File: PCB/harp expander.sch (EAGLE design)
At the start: 132 parts, among them IC1 XMEGA-A1TQFP, IC14 SN74LVC1G125DBVT, IC2 USBLC6-2SC6, IC3 FT232RL, IC4 TLV70033DDCR, IC5 TLV70033DDCR, IC6 SI8610BC-B-IS, IC7 SN74LVC1G125DBVT, T10 BC850, T11 BC850, T12 BC850, T13 BC850, T2 BC850, T3 BC850, T4 BC850, T5 BC850, T6 BC850, T7 BC850, T8 BC850, T9 BC850, U1 744245X, U2 744245X

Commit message: Minor corrections.
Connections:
- net IO_BUTTON0 renamed AUX_IN0
- net IO_BUTTON1 renamed AUX_IN1
- net PD0 renamed IO4_UC
- net PD1 renamed IO3_UC
- net PD2 renamed IO2_UC
- net PD3 renamed IO1_UC
- net PD4 renamed IO0_UC
- net PE0 renamed IO5_UC
- net PE1 renamed IO6_UC
- net PE2 renamed IO7_UC
- net PE3 renamed IO8_UC
- net PE4 renamed IO9_UC
- net USER_BUTTON_1 renamed AUX_IN1_UC
- removed net USER_BUTTON_0: IC1.PA1(ADCA1), IC14A.O
- new net AUX_IN0_UC: IC1.PA1(ADCA1), IC1.PE2(OC0C/RXD0), IC14A.O
- new net N$166: IC1.PF6(RXD1/MISO)

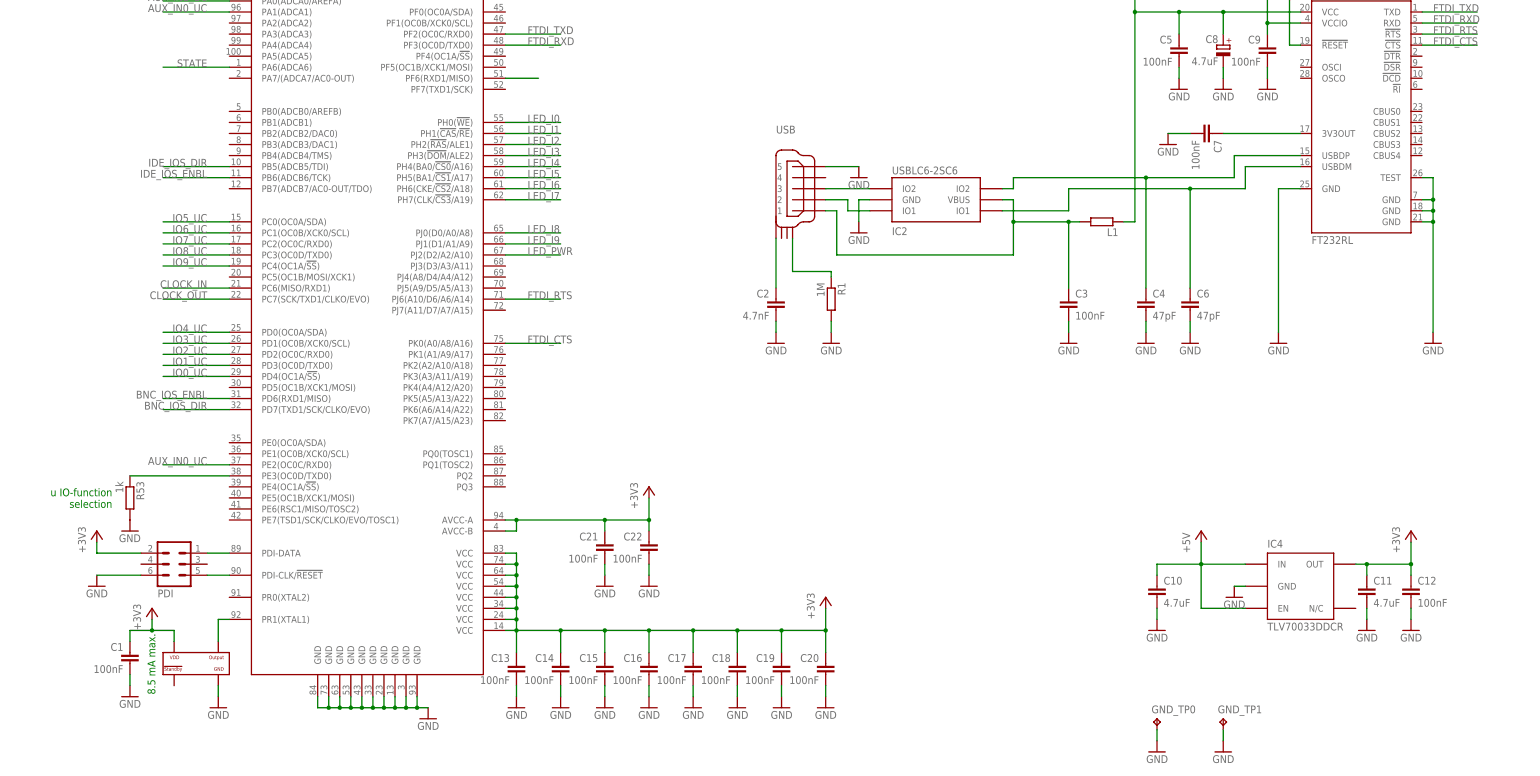
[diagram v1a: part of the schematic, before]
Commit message: Added ability to connect to a Teensy/Arduino and to read rotary encoders.
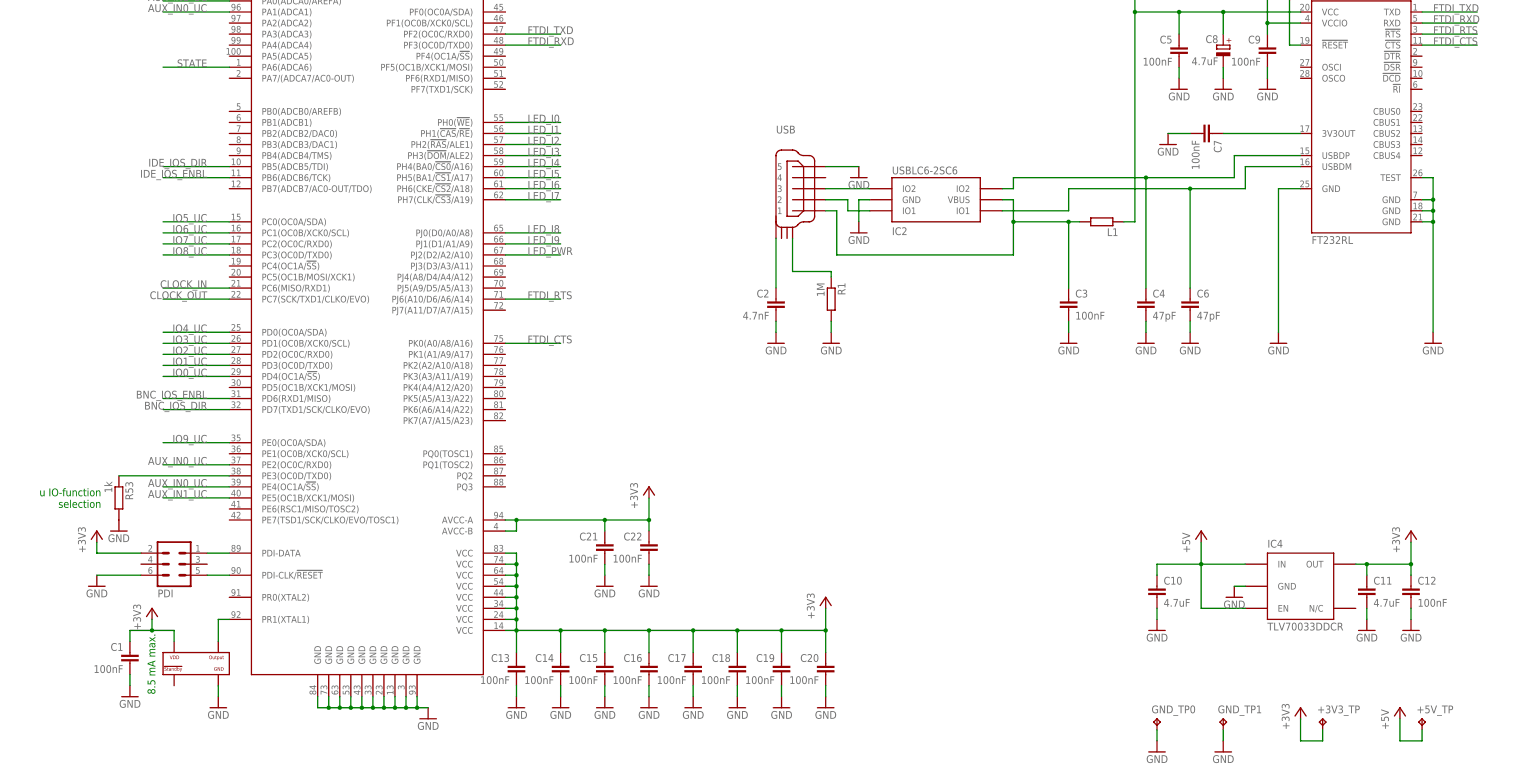
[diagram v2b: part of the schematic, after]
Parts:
- added +3V3_TP, +5V_TP: TPPAD1-13, testpad:TPPAD1-13
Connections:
- removed net N$166: IC1.PF6(RXD1/MISO)
- net +3V3: now also +3V3_TP.TP
- net +5V: now also +5V_TP.TP
- net AUX_IN0_UC: now also IC1.PE4(OC1A/!SS!)
- net AUX_IN1_UC: now also IC1.PE5(OC1B/XCK1/MOSI)
- net IO9_UC: now also IC1.PE0(OC0A/SDA); no longer IC1.PC4(OC1A/!SS!)
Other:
- moved on the sheet: R53
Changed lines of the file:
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@@
 </part>
 <part name="GND61" library="supply1" deviceset="GND" device=""/>
+<part name="+3V3_TP" library="testpad" library_urn="urn:adsk.eagle:library:385" deviceset="TP" device="PAD1-13" package3d_urn="urn:adsk.eagle:package:27946/1">
+<attribute name="MPN" value="n.a."/>
+</part>
+<part name="+3V19" library="supply1" library_urn="urn:adsk.eagle:library:371" deviceset="+3V3" device=""/>
+<part name="+5V_TP" library="testpad" library_urn="urn:adsk.eagle:library:385" deviceset="TP" device="PAD1-13" package3d_urn="urn:adsk.eagle:package:27946/1">
+<attribute name="MPN" value="n.a."/>
+</part>
+<part name="P+5" library="supply1" deviceset="+5V" device=""/>
 </parts>
 <sheets>
@@
 <text x="54.102" y="51.308" size="1.778" layer="91" rot="R90">8.5 mA max.</text>
 <text x="657.86" y="332.74" size="1.778" layer="91">SBH11-PBPC-D05-RA-BK</text>
-<text x="44.196" y="94.234" size="1.778" layer="91" align="bottom-right">u IO-function
+<text x="41.656" y="94.234" size="1.778" layer="91" align="bottom-right">u IO-function
 selection</text>
 </plain>
@@
 <attribute name="VALUE" x="548.64" y="274.32" size="1.778" layer="96"/>
 </instance>
-<instance part="R53" gate="G$1" x="48.26" y="96.52" smashed="yes" rot="R270">
-<attribute name="NAME" x="49.7586" y="100.33" size="1.778" layer="95" rot="R270"/>
-<attribute name="VALUE" x="44.958" y="100.33" size="1.778" layer="96" rot="R270"/>
-<attribute name="MPN" x="48.26" y="96.52" size="1.778" layer="96" rot="R270" display="off"/>
+<instance part="R53" gate="G$1" x="45.72" y="96.52" smashed="yes" rot="R270">
+<attribute name="NAME" x="47.2186" y="100.33" size="1.778" layer="95" rot="R270"/>
+<attribute name="VALUE" x="42.418" y="100.33" size="1.778" layer="96" rot="R270"/>
+<attribute name="MPN" x="45.72" y="96.52" size="1.778" layer="96" rot="R270" display="off"/>
+</instance>
+<instance part="GND61" gate="1" x="45.72" y="88.9" smashed="yes">
+<attribute name="VALUE" x="43.18" y="86.36" size="1.778" layer="96"/>
+</instance>
+<instance part="+3V3_TP" gate="G$1" x="322.58" y="45.72" smashed="yes">
+<attribute name="NAME" x="321.31" y="46.99" size="1.778" layer="95"/>
+<attribute name="TP_SIGNAL_NAME" x="323.85" y="44.45" size="1.778" layer="97"/>
+<attribute name="MPN" x="322.58" y="45.72" size="1.778" layer="96" display="off"/>
+</instance>
+<instance part="+3V19" gate="G$1" x="317.5" y="48.26" smashed="yes">
+<attribute name="VALUE" x="314.96" y="43.18" size="1.778" layer="96" rot="R90"/>
+</instance>
+<instance part="+5V_TP" gate="G$1" x="345.44" y="45.72" smashed="yes">
+<attribute name="NAME" x="344.17" y="46.99" size="1.778" layer="95"/>
+<attribute name="TP_SIGNAL_NAME" x="346.71" y="44.45" size="1.778" layer="97"/>
+<attribute name="MPN" x="345.44" y="45.72" size="1.778" layer="96" display="off"/>
 </instance>
-<instance part="GND61" gate="1" x="48.26" y="88.9" smashed="yes">
-<attribute name="VALUE" x="45.72" y="86.36" size="1.778" layer="96"/>
+<instance part="P+5" gate="1" x="340.36" y="48.26" smashed="yes">
+<attribute name="VALUE" x="337.82" y="43.18" size="1.778" layer="96" rot="R90"/>
 </instance>
 </instances>
@@
 <junction x="492.76" y="421.64"/>
 </segment>
+<segment>
+<pinref part="P+5" gate="1" pin="+5V"/>
+<wire x1="340.36" y1="45.72" x2="340.36" y2="40.64" width="0.1524" layer="91"/>
+<wire x1="340.36" y1="40.64" x2="345.44" y2="40.64" width="0.1524" layer="91"/>
+<pinref part="+5V_TP" gate="G$1" pin="TP"/>
+<wire x1="345.44" y1="40.64" x2="345.44" y2="43.18" width="0.1524" layer="91"/>
+</segment>
 </net>
 <net name="N$2" class="0">
@@
 <label x="66.04" y="210.82" size="1.778" layer="95" rot="MR0"/>
 </segment>
+<segment>
+<pinref part="IC1" gate="G$1" pin="PE5(OC1B/XCK1/MOSI)"/>
+<wire x1="71.12" y1="96.52" x2="55.88" y2="96.52" width="0.1524" layer="91"/>
+<label x="66.04" y="96.52" size="1.778" layer="95" rot="MR0"/>
+</segment>
 </net>
 <net name="AUX_IN0_UC" class="0">
@@
 <label x="66.04" y="104.14" size="1.778" layer="95" rot="MR0"/>
 </segment>
+<segment>
+<pinref part="IC1" gate="G$1" pin="PE4(OC1A/!SS!)"/>
+<wire x1="71.12" y1="99.06" x2="55.88" y2="99.06" width="0.1524" layer="91"/>
+<label x="66.04" y="99.06" size="1.778" layer="95" rot="MR0"/>
+</segment>
 </net>
 <net name="+3V3" class="0">
@@
 <wire x1="500.38" y1="284.48" x2="500.38" y2="287.02" width="0.1524" layer="91"/>
 </segment>
+<segment>
+<pinref part="+3V19" gate="G$1" pin="+3V3"/>
+<wire x1="317.5" y1="45.72" x2="317.5" y2="40.64" width="0.1524" layer="91"/>
+<wire x1="317.5" y1="40.64" x2="322.58" y2="40.64" width="0.1524" layer="91"/>
+<pinref part="+3V3_TP" gate="G$1" pin="TP"/>
+<wire x1="322.58" y1="40.64" x2="322.58" y2="43.18" width="0.1524" layer="91"/>
+</segment>
 </net>
 <net name="N$175" class="0">
@@
 </segment>
 <segment>
-<wire x1="71.12" y1="149.86" x2="55.88" y2="149.86" width="0.1524" layer="91"/>
-<label x="66.04" y="149.86" size="1.778" layer="95" rot="MR0"/>
-<pinref part="IC1" gate="G$1" pin="PC4(OC1A/!SS!)"/>
+<pinref part="IC1" gate="G$1" pin="PE0(OC0A/SDA)"/>
+<wire x1="71.12" y1="109.22" x2="55.88" y2="109.22" width="0.1524" layer="91"/>
+<label x="66.04" y="109.22" size="1.778" layer="95" rot="MR0"/>
 </segment>
 </net>
@@
 <pinref part="IC1" gate="G$1" pin="PE3(OC0D/TXD0)"/>
 <pinref part="R53" gate="G$1" pin="1"/>
-<wire x1="71.12" y1="101.6" x2="48.26" y2="101.6" width="0.1524" layer="91"/>
-</segment>
-</net>
-<net name="N$166" class="0">
-<segment>
-<pinref part="IC1" gate="G$1" pin="PF6(RXD1/MISO)"/>
-<wire x1="134.62" y1="193.04" x2="142.24" y2="193.04" width="0.1524" layer="91"/>
+<wire x1="71.12" y1="101.6" x2="45.72" y2="101.6" width="0.1524" layer="91"/>
 </segment>
 </net>

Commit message: Added ability to be used as a clock generator.
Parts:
- removed JP1: CLCK Jumper, jumper:JP2E
- added C35, C36: 100nF, rcl:C-EUC0402
- added IC8, IC9: SN74LVC1G125DBVT, 74xx-little-de:74AHC1G125DBV
- added R54, R55: 10k, rcl:R-EU_R0402
- R53: value 1k -> 10
- renumbered IC14 to IC10
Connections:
- new net EN_CLOCK_IN: IC1.PK2(A2/A10/A18), IC8A.OE, R54.1
- new net EN_CLOCK_OUT: IC1.PK1(A1/A9/A17), IC9A.OE, R55.1
- net +3V3: now also C35.1, C36.1, IC8P.VCC, IC9P.VCC, R55.2
- net CLOCK_IN: now also IC8A.I; no longer JP1.3
- net CLOCK_OUT: now also IC9A.I; no longer JP1.1
- net GND: now also C35.2, C36.2, IC8P.GND, IC9P.GND, R54.2
- net N$43: now also IC8A.O, IC9A.O; no longer JP1.2
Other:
- moved on the sheet: C23, C24, CLKIN, IC5, R2, R3

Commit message: Minor corrections on layout and schematics.
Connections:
- net AUX_IN0_UC: no longer IC1.PA1(ADCA1)
- net AUX_IN1_UC: no longer IC1.PA0(ADCA0/AREFA)
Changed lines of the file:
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@@
 <pinref part="CLKIN" gate="G$1" pin="4"/>
 <pinref part="R3" gate="G$1" pin="2"/>
-<wire x1="104.14" y1="426.72" x2="147.32" y2="426.72" width="0.1524" layer="91"/>
+<wire x1="101.6" y1="426.72" x2="147.32" y2="426.72" width="0.1524" layer="91"/>
 <wire x1="147.32" y1="426.72" x2="228.6" y2="426.72" width="0.1524" layer="91"/>
 <wire x1="228.6" y1="426.72" x2="236.22" y2="426.72" width="0.1524" layer="91"/>
 <wire x1="228.6" y1="429.26" x2="228.6" y2="426.72" width="0.1524" layer="91"/>
 <junction x="228.6" y="426.72"/>
-<label x="104.14" y="426.72" size="1.778" layer="95"/>
+<label x="101.6" y="426.72" size="1.778" layer="95"/>
 <wire x1="147.32" y1="421.64" x2="147.32" y2="426.72" width="0.1524" layer="91"/>
 <junction x="147.32" y="426.72"/>
@@
 </segment>
 <segment>
-<wire x1="129.54" y1="386.08" x2="104.14" y2="386.08" width="0.1524" layer="91"/>
-<label x="104.14" y="386.08" size="1.778" layer="95"/>
+<wire x1="129.54" y1="386.08" x2="101.6" y2="386.08" width="0.1524" layer="91"/>
+<label x="101.6" y="386.08" size="1.778" layer="95"/>
 <pinref part="IC9" gate="A" pin="I"/>
 </segment>
@@
 </segment>
 <segment>
-<pinref part="IC1" gate="G$1" pin="PA0(ADCA0/AREFA)"/>
-<wire x1="71.12" y1="210.82" x2="55.88" y2="210.82" width="0.1524" layer="91"/>
-<label x="66.04" y="210.82" size="1.778" layer="95" rot="MR0"/>
-</segment>
-<segment>
 <pinref part="IC1" gate="G$1" pin="PE5(OC1B/XCK1/MOSI)"/>
 <wire x1="71.12" y1="96.52" x2="55.88" y2="96.52" width="0.1524" layer="91"/>
@@
 <label x="457.2" y="330.2" size="1.778" layer="95"/>
 <pinref part="IC10" gate="A" pin="O"/>
-</segment>
-<segment>
-<pinref part="IC1" gate="G$1" pin="PA1(ADCA1)"/>
-<wire x1="71.12" y1="208.28" x2="55.88" y2="208.28" width="0.1524" layer="91"/>
-<label x="66.04" y="208.28" size="1.778" layer="95" rot="MR0"/>
 </segment>
 <segment>
@@
 <pinref part="IC8" gate="A" pin="OE"/>
 <wire x1="139.7" y1="416.56" x2="124.46" y2="416.56" width="0.1524" layer="91"/>
-<label x="104.14" y="416.56" size="1.778" layer="95"/>
+<label x="101.6" y="416.56" size="1.778" layer="95"/>
 <pinref part="R54" gate="G$1" pin="1"/>
-<wire x1="124.46" y1="416.56" x2="104.14" y2="416.56" width="0.1524" layer="91"/>
+<wire x1="124.46" y1="416.56" x2="101.6" y2="416.56" width="0.1524" layer="91"/>
 <wire x1="124.46" y1="414.02" x2="124.46" y2="416.56" width="0.1524" layer="91"/>
 <junction x="124.46" y="416.56"/>

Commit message: Added filtering on inputs and reset lines to prevent erroneous behavior in noisy environments.
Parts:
- removed C8: 4.7uF, rcl:CPOL-EUA/3216-18W
- removed R1: 1M, rcl:R-EU_R0402
- removed R18: 10k, rcl:R-EU_R0402
- added C39: 100u 25V, rcl:CPOL-EUTT2D6
- added C40: 100nF, rcl:C-EUC0402
- added C41, C42, C43, C44, C45, C46, C47, C48, C49, C50, C51: 330pF, rcl:C-EUC0402
- added C52: 4.7uF, rcl:C-EUC0603
- added R56, R57, R58, R59, R60, R61, R62, R63, R64, R65, R66, R67, R68: 10k, rcl:R-EU_R0402
- added R69: 100R, rcl:R-EU_R0603
- added U3: 74HCT125SO14, harp input expander:74HCT125SO14
- BNC0, BNC1, BNC2, BNC3, BNC4, PDI, SV1: NOTES (none) -> -; TYPE (none) -> TH
- C1, C10, C11, C12, C13, C14, C15, C16, C17, C18, C19, C2, C20, C21, C22, C23, C24, C25, C26, C27, C28, C29, C3, C30, C31, C32, C33, C34, C35, C36, C37, C38, C4, C5, C6, C7, C9, IC10, IC4, IC7, IC8, IC9, L1, R10, R11, R12, R13, R14, R15, R16, R17, R19, R2, R20, R21, R22, R23, R24, R25, R26, R27, R28, R29, R3, R30, R31, R32, R33, R34, R35, R36, R37, R38, R39, R4, R40, R41, R42, R43, R44, R45, R46, R47, R48, R49, R5, R50, R51, R52, R54, R55, R6, R7, R8, R9: NOTES (none) -> -; TYPE (none) -> SMD
- CLKIN, CLKOUT: device CNP-connectors:STEREO_JACK -> harp input expander:STEREO_JACK; NOTES (none) -> -; TYPE (none) -> SMD
- IC1, IC3, T10, T11, T12, T13, T2, T3, T4, T5, T6, T7, T8, T9, U1, U2: TYPE (none) -> SMD
- IC2: device CNP 2:USBLC6-2 -> harp input expander:USBLC6-2; NOTES (none) -> -; TYPE (none) -> SMD
- IC5: device CNP:TLV700XX -> harp input expander:TLV700XX; NOTES (none) -> -; TYPE (none) -> SMD
- IC6: device CNP-ics 2:SI8610 -> harp input expander:SI8610; NOTES (none) -> -; TYPE (none) -> SMD
- LED0, LED1, LED2, LED3, LED4, LED5: value 569-0112-100 -> RED_LEDs; device jonnew:LED_2X_VERTICAL -> harp input expander:LED_2X_VERTICAL; NOTES (none) -> -; TYPE (none) -> TH
- OSC: device CNP-miscellaneous:OSCILLATOR -> harp input expander:OSCILLATOR; MPN DSC1001CI5-032.0000T -> O 32,0-JT32C-A-K-3,3-LF; NOTES (none) -> Alternative: DSC1001CI5-032.0000T; TYPE (none) -> SMD
- R53: value 10 -> 10k; MPN CRCW04021K00FKED -> CRCW040210K0FKED; NOTES (none) -> -; TYPE (none) -> SMD
- USB: device CNP-connectors:USB_MINI_B -> harp input expander:USB_MINI_B; NOTES (none) -> -; TYPE (none) -> SMD
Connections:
- removed net N$175: IC3.!RESET, R18.2
- new net N$140: R61.1, U1.B5
- new net N$143: R60.1, U1.B6
- new net N$145: R59.1, U1.B7
- new net N$146: R56.1, U1.A7
- new net N$165: R57.1, U1.A6
- new net N$166: R58.1, U1.A5
- new net N$167: R62.1, U2.A7
- new net N$169: R63.1, U2.A6
- new net N$170: R64.1, U2.A5
- new net N$171: R67.1, U2.B5
- new net N$172: R66.1, U2.B6
- new net N$173: R65.1, U2.B7
- new net U_BNC_IOS_DIR: IC1.PD7(TXD1/SCK/CLKO/EVO), U3.1A
- new net U_BNC_IOS_ENBL: IC1.PD6(RXD1/MISO), U3.2A
- new net U_IDE_IOS_DIR: IC1.PB5(ADCB5/TDI), U3.3A
- new net U_IDE_IOS_ENBL: IC1.PB6(ADCB6/TCK), U3.4A
- net +3V3: now also IC1.PF6(RXD1/MISO), R68.2; no longer R18.1
- net +5V: now also C39.+, C40.1, C52.1, U3.VCC; no longer C8.+
- net BNC_IOS_DIR: now also U3.1Y; no longer IC1.PD7(TXD1/SCK/CLKO/EVO)
- net BNC_IOS_ENBL: now also U3.2B; no longer IC1.PD6(RXD1/MISO)
- net GND: now also C39.-, C40.2, C41.2, C42.2, C43.2, C44.2, C45.2, C46.2, C47.2, C48.2, C49.2, C50.2, C51.2, C52.2, R56.2, R57.2, R58.2, R59.2, R60.2, R61.2, R62.2, R63.2, R64.2, R65.2, R66.2, R67.2, R69.2, U3.!1OE, U3.!2OE, U3.!3OE, U3.!4OE, U3.GND; no longer C8.-, R1.2
- net IDE_IOS_DIR: now also U3.3Y; no longer IC1.PB5(ADCB5/TDI)
- net IDE_IOS_ENBL: now also U3.4Y; no longer IC1.PB6(ADCB6/TCK)
- net N$114: now also C46.1
- net N$115: now also C45.1
- net N$116: now also C44.1
- net N$122: now also C43.1
- net N$142: now also C42.1
- net N$152: now also C41.1
- net N$6: now also C50.1
- net N$61: now also R69.1; no longer R1.1
- net N$68: now also C49.1
- net N$69: now also C48.1
- net N$97: now also C47.1
- net PDI_CLK: now also C51.1, R68.1
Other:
- note added: "R53 u IO-function selection"
- note added: "version control pin"
- note removed: "u IO-function selection"
- moved on the sheet: BNC0, BNC1, BNC2, BNC3, BNC4, C1, C13, C14, C15, C16, C17, C18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
